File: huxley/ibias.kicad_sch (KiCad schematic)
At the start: 24 parts, among them J21 61300211121, J25 61300211121, J26 61300211121, J27 61300211121, J28 61300211121, J29 61300211121, J30 61300211121, J31 61300211121, U2 LM134H, U4 TMUX1112PWR, U5 TMUX1112PWR

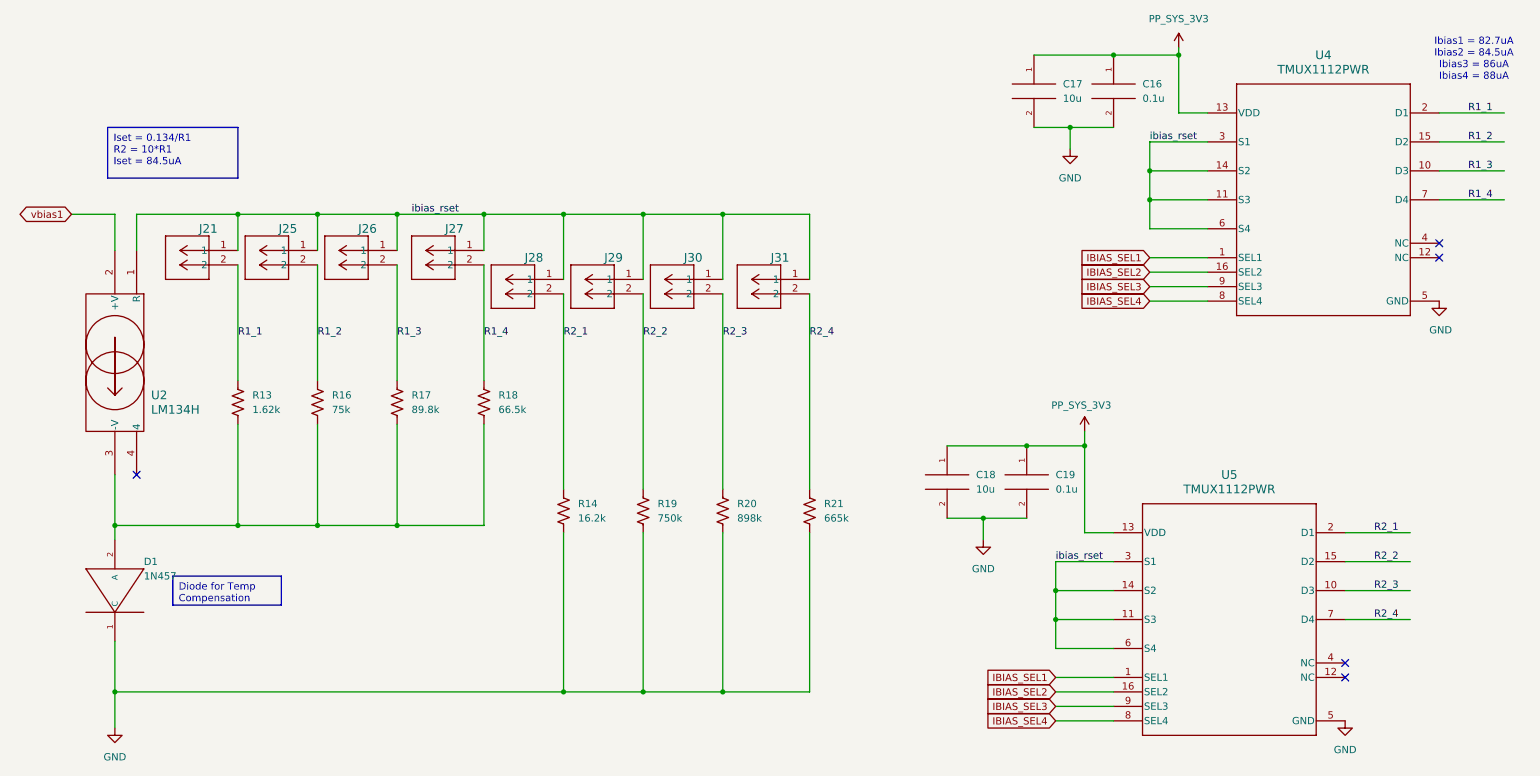
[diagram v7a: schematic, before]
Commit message: fixed all bad refs; replaced analog discovery connector; change level shifter 3v3 to from analog discovery
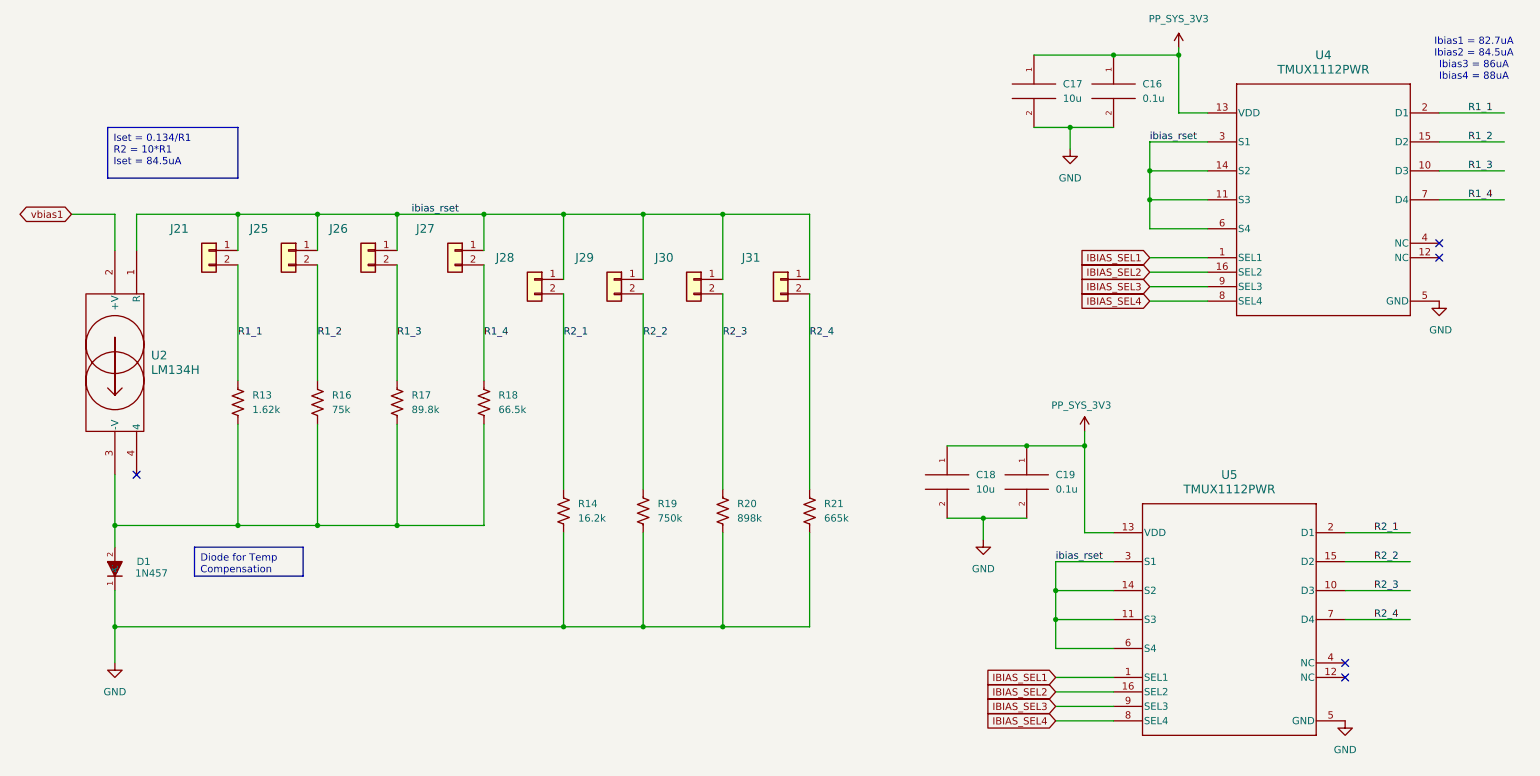
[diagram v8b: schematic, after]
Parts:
- D1: footprint 726_footprints:DIO_1N457 -> 0_726_footprints:DIO_1N457; symbol _PHASE:1N457 -> 0_PHASE:1N457
- J21, J25, J26, J27, J28, J29, J30, J31: footprint 726_footprints:CONN_61300211121_WRE -> Connector_PinHeader_2.54mm:PinHeader_1x02_P2.54mm_Vertical; symbol _PHASE:61300211121 -> Connector_Generic:Conn_01x02
- U2: footprint 726_footprints:lm134 -> 0_726_footprints:lm134; symbol _PHASE:LM134H -> 0_PHASE:LM134H
- U4, U5: symbol _PHASE:TMUX1112PWR -> 0_PHASE:TMUX1112PWR
